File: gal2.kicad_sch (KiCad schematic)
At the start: 1 part, among them IC1 D65101GD055

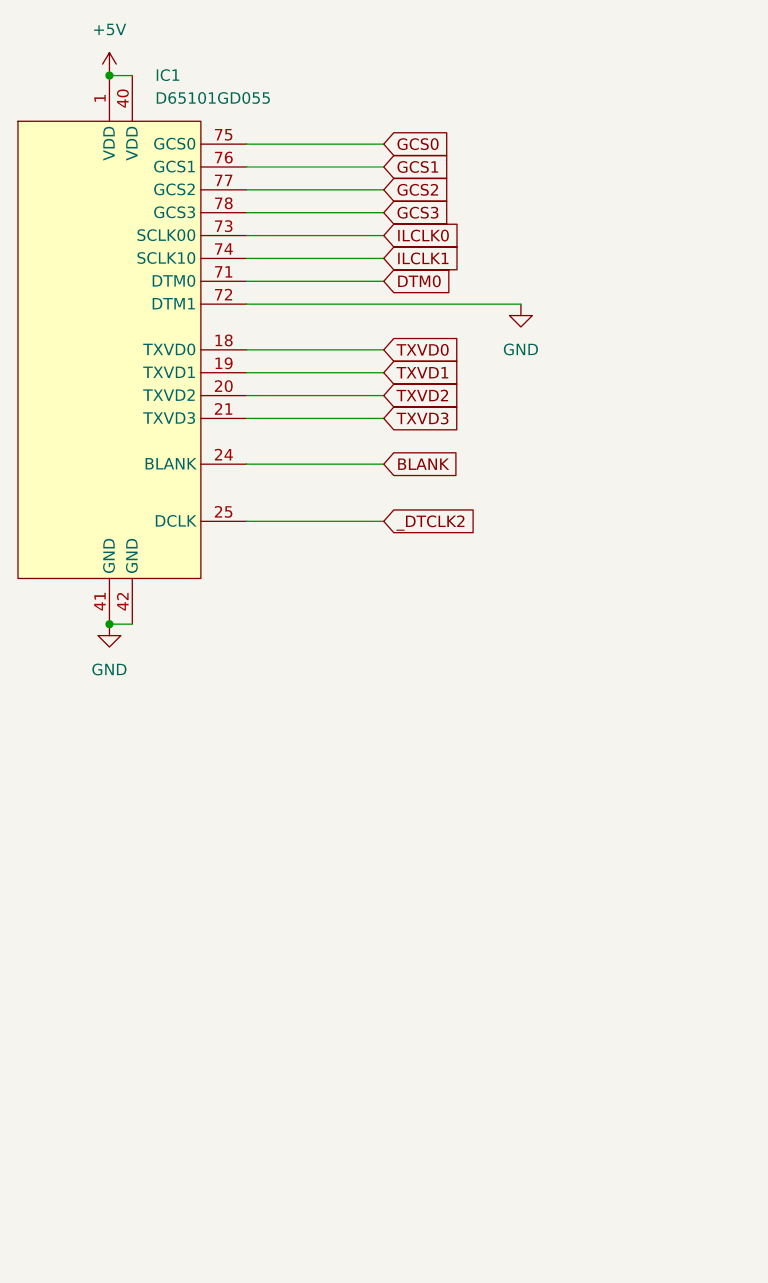
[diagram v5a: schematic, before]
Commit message: schematic: wire IC1 pin 84-91 to CN4. pcb: add lines around IC1
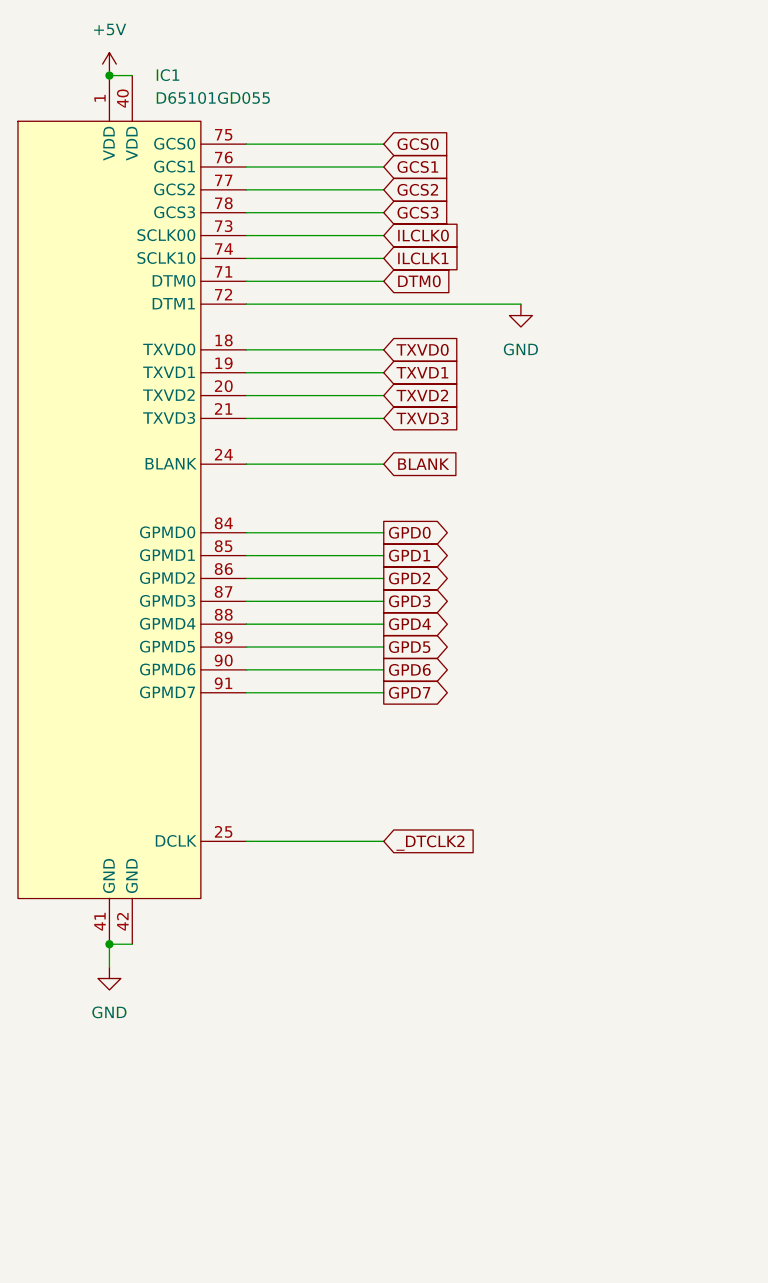
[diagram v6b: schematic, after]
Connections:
- new net GPD0: IC1.84 (GPMD0)
- new net GPD1: IC1.85 (GPMD1)
- new net GPD2: IC1.86 (GPMD2)
- new net GPD3: IC1.87 (GPMD3)
- new net GPD4: IC1.88 (GPMD4)
- new net GPD5: IC1.89 (GPMD5)
- new net GPD6: IC1.90 (GPMD6)
- new net GPD7: IC1.91 (GPMD7)
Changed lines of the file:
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@@
     (comment 1 "VA1回路図 P.252")
   )
+  (junction (at 46.99 137.16) (diameter 0) (color 0 0 0 0)
+  )
   (junction (at 46.99 40.64) (diameter 0) (color 0 0 0 0)
   )
-  (junction (at 46.99 101.6) (diameter 0) (color 0 0 0 0)
+  (wire (pts (xy 62.23 93.98) (xy 77.47 93.98))
+    (stroke (width 0) (type default))
+  )
+  (wire (pts (xy 62.23 96.52) (xy 77.47 96.52))
+    (stroke (width 0) (type default))
   )
   (wire (pts (xy 62.23 53.34) (xy 77.47 53.34))
@@
     (stroke (width 0) (type default))
   )
-  (wire (pts (xy 62.23 90.17) (xy 77.47 90.17))
+  (wire (pts (xy 62.23 101.6) (xy 77.47 101.6))
+    (stroke (width 0) (type default))
+  )
+  (wire (pts (xy 62.23 125.73) (xy 77.47 125.73))
+    (stroke (width 0) (type default))
+  )
+  (wire (pts (xy 46.99 139.7) (xy 46.99 137.16))
+    (stroke (width 0) (type default))
+  )
+  (wire (pts (xy 62.23 109.22) (xy 77.47 109.22))
     (stroke (width 0) (type default))
   )
@@
     (stroke (width 0) (type default))
   )
+  (wire (pts (xy 62.23 104.14) (xy 77.47 104.14))
+    (stroke (width 0) (type default))
+  )
   (wire (pts (xy 62.23 55.88) (xy 77.47 55.88))
     (stroke (width 0) (type default))
   )
-  (wire (pts (xy 46.99 101.6) (xy 49.53 101.6))
+  (wire (pts (xy 62.23 99.06) (xy 77.47 99.06))
+    (stroke (width 0) (type default))
+  )
+  (wire (pts (xy 46.99 137.16) (xy 49.53 137.16))
+    (stroke (width 0) (type default))
+  )
+  (wire (pts (xy 62.23 106.68) (xy 77.47 106.68))
     (stroke (width 0) (type default))
   )
@@
     (stroke (width 0) (type default))
   )
+  (wire (pts (xy 62.23 91.44) (xy 77.47 91.44))
+    (stroke (width 0) (type default))
+  )
   (wire (pts (xy 62.23 58.42) (xy 77.47 58.42))
     (stroke (width 0) (type default))
@@
     )
   )
+  (global_label "GPD3" (shape output) (at 77.47 99.06 0) (fields_autoplaced)
+    (effects (font (size 1.27 1.27)) (justify left))
+    (property "Intersheetrefs" "${INTERSHEET_REFS}" (at 85.4747 99.06 0)
+      (effects (font (size 1.27 1.27)) (justify left) hide)
+    )
+  )
   (global_label "GCS0" (shape input) (at 77.47 48.26 0) (fields_autoplaced)
     (effects (font (size 1.27 1.27)) (justify left))
@@
     )
   )
+  (global_label "GPD5" (shape output) (at 77.47 104.14 0) (fields_autoplaced)
+    (effects (font (size 1.27 1.27)) (justify left))
+    (property "Intersheetrefs" "${INTERSHEET_REFS}" (at 85.4747 104.14 0)
+      (effects (font (size 1.27 1.27)) (justify left) hide)
+    )
+  )
   (global_label "TXVD1" (shape input) (at 77.47 73.66 0) (fields_autoplaced)
     (effects (font (size 1.27 1.27)) (justify left))
@@
     )
   )
-  (global_label "_DTCLK2" (shape input) (at 77.47 90.17 0) (fields_autoplaced)
-    (effects (font (size 1.27 1.27)) (justify left))
-    (property "Intersheetrefs" "${INTERSHEET_REFS}" (at 88.438 90.17 0)
+  (global_label "_DTCLK2" (shape input) (at 77.47 125.73 0) (fields_autoplaced)
+    (effects (font (size 1.27 1.27)) (justify left))
+    (property "Intersheetrefs" "${INTERSHEET_REFS}" (at 88.438 125.73 0)
+      (effects (font (size 1.27 1.27)) (justify left) hide)
+    )
+  )
+  (global_label "GPD6" (shape output) (at 77.47 106.68 0) (fields_autoplaced)
+    (effects (font (size 1.27 1.27)) (justify left))
+    (property "Intersheetrefs" "${INTERSHEET_REFS}" (at 85.4747 106.68 0)
       (effects (font (size 1.27 1.27)) (justify left) hide)
     )
@@
     )
   )
+  (global_label "GPD0" (shape output) (at 77.47 91.44 0) (fields_autoplaced)
+    (effects (font (size 1.27 1.27)) (justify left))
+    (property "Intersheetrefs" "${INTERSHEET_REFS}" (at 85.4747 91.44 0)
+      (effects (font (size 1.27 1.27)) (justify left) hide)
+    )
+  )
+  (global_label "GPD4" (shape output) (at 77.47 101.6 0) (fields_autoplaced)
+    (effects (font (size 1.27 1.27)) (justify left))
+    (property "Intersheetrefs" "${INTERSHEET_REFS}" (at 85.4747 101.6 0)
+      (effects (font (size 1.27 1.27)) (justify left) hide)
+    )
+  )
+  (global_label "GPD2" (shape output) (at 77.47 96.52 0) (fields_autoplaced)
+    (effects (font (size 1.27 1.27)) (justify left))
+    (property "Intersheetrefs" "${INTERSHEET_REFS}" (at 85.4747 96.52 0)
+      (effects (font (size 1.27 1.27)) (justify left) hide)
+    )
+  )
+  (global_label "GPD1" (shape output) (at 77.47 93.98 0) (fields_autoplaced)
+    (effects (font (size 1.27 1.27)) (justify left))
+    (property "Intersheetrefs" "${INTERSHEET_REFS}" (at 85.4747 93.98 0)
+      (effects (font (size 1.27 1.27)) (justify left) hide)
+    )
+  )
   (global_label "GCS3" (shape input) (at 77.47 55.88 0) (fields_autoplaced)
     (effects (font (size 1.27 1.27)) (justify left))
@@
     (effects (font (size 1.27 1.27)) (justify left))
     (property "Intersheetrefs" "${INTERSHEET_REFS}" (at 86.8657 60.96 0)
+      (effects (font (size 1.27 1.27)) (justify left) hide)
+    )
+  )
+  (global_label "GPD7" (shape output) (at 77.47 109.22 0) (fields_autoplaced)
+    (effects (font (size 1.27 1.27)) (justify left))
+    (property "Intersheetrefs" "${INTERSHEET_REFS}" (at 85.4747 109.22 0)
       (effects (font (size 1.27 1.27)) (justify left) hide)
     )
@@
     )
   )
-  (symbol (lib_id "power:GND") (at 46.99 101.6 0) (unit 1)
+  (symbol (lib_id "power:GND") (at 46.99 139.7 0) (unit 1)
     (in_bom yes) (on_board yes) (dnp no) (fields_autoplaced)
-    (property "Reference" "#PWR029" (at 46.99 107.95 0)
-      (effects (font (size 1.27 1.27)) hide)
-    )
-    (property "Value" "GND" (at 46.99 106.68 0)
+    (property "Reference" "#PWR029" (at 46.99 146.05 0)
+      (effects (font (size 1.27 1.27)) hide)
+    )
+    (property "Value" "GND" (at 46.99 144.78 0)
       (effects (font (size 1.27 1.27)))
     )
-    (property "Footprint" "" (at 46.99 101.6 0)
-      (effects (font (size 1.27 1.27)) hide)
-    )
-    (property "Datasheet" "" (at 46.99 101.6 0)
+    (property "Footprint" "" (at 46.99 139.7 0)
+      (effects (font (size 1.27 1.27)) hide)
+    )
+    (property "Datasheet" "" (at 46.99 139.7 0)
       (effects (font (size 1.27 1.27)) hide)
     )
@@
     (pin "20")
     (pin "24")
+    (pin "85")
+    (pin "87")
+    (pin "91")
+    (pin "88")
+    (pin "90")
+    (pin "89")
+    (pin "84")
+    (pin "86")
     (instances
       (project "88va2-circuit"

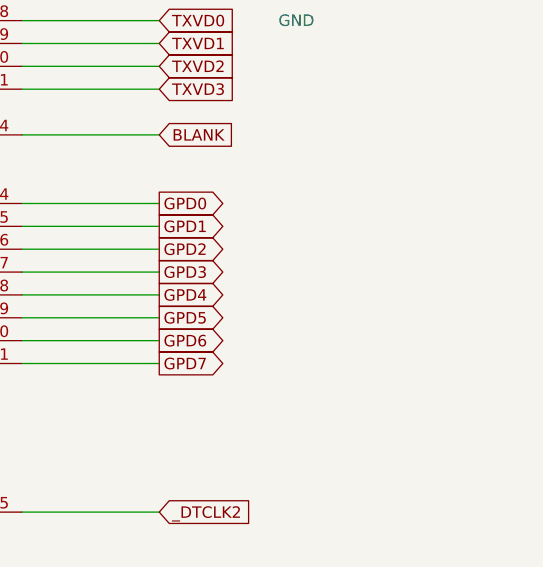
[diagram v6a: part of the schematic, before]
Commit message: schematic: add comments
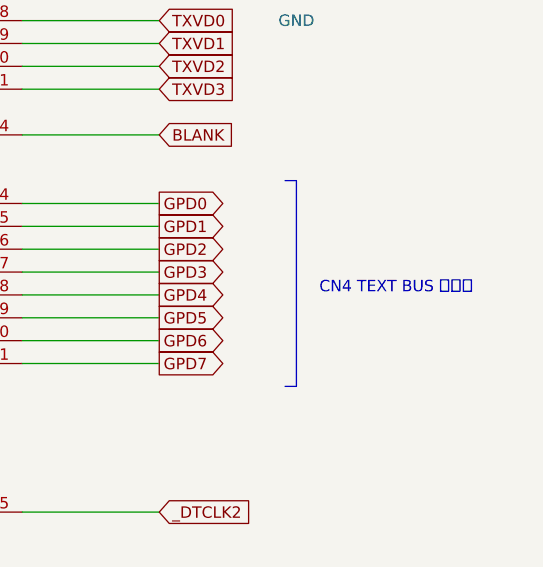
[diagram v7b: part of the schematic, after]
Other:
- note added: "CN4 TEXT BUS へ接続"
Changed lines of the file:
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@@
+    (stroke (width 0) (type default))
+  )
+  (polyline (pts (xy 91.44 111.76) (xy 92.71 111.76))
+    (stroke (width 0) (type default))
+  )
+  (polyline (pts (xy 92.71 111.76) (xy 92.71 88.9))
     (stroke (width 0) (type default))
   )
@@
     (stroke (width 0) (type default))
   )
+  (polyline (pts (xy 91.44 88.9) (xy 92.71 88.9))
+    (stroke (width 0) (type default))
+  )
   (wire (pts (xy 62.23 55.88) (xy 77.47 55.88))
     (stroke (width 0) (type default))
@@
     (stroke (width 0) (type default))
   )
+  (text "CN4 TEXT BUS へ接続" (at 95.25 101.6 0)
+    (effects (font (size 1.27 1.27)) (justify left bottom))
+  )
   (global_label "ILCLK0" (shape input) (at 77.47 58.42 0) (fields_autoplaced)
